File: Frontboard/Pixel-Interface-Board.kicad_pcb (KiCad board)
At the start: 2 copper layers, 29 parts, among them IC1 ATTINY85-P, P1 CONN_02X20, SW1 SW_PUSH, SW10 SW_PUSH, SW11 SW_PUSH, SW12 SW_PUSH, SW2 SW_PUSH, SW3 SW_PUSH, SW4 SW_PUSH, SW5 SW_PUSH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

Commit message: Directories moved, .gitignore added.  Major changes to Frontboard design.  Header was completely backwards, fixed now, pins re-arranged. Table coming shortly.
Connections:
- P1 pad 1: /X -> GND
- P1 pad 10: /R -> (no net)
- P1 pad 11: GND -> (no net)
- P1 pad 13: (no net) -> /Y
- P1 pad 15: (no net) -> /SELECT
- P1 pad 16: GND -> /L
- P1 pad 18: (no net) -> /R
- P1 pad 19: (no net) -> /START
- P1 pad 28: /LEFT -> (no net)
- P1 pad 30: /RIGHT -> GND
- P1 pad 32: GND -> /LEFT
- P1 pad 34: (no net) -> GND
- P1 pad 36: (no net) -> /RIGHT
- P1 pad 4: /START -> (no net)
- P1 pad 6: /SELECT -> (no net)
- P1 pad 7: GND -> /X
- P1 pad 8: /L -> (no net)
- P1 pad 9: /Y -> GND
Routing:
- net /R: track 95.4 -> 333.9 mm
- net GND: track 155.1 -> 55.3 mm
- net /RIGHT: track 137.5 -> 204.8 mm
- net /A: track 118.8 -> 137.4 mm
- net /B: track 123.1 -> 139.0 mm
- net /Y: track 104.4 -> 116.6 mm
- net /L: track 60.7 -> 72.6 mm
- net /LEFT: track 153.3 -> 162.0 mm
- net /START: track 151.1 -> 143.8 mm
- net /SELECT: track 148.8 -> 144.5 mm
- net /X: track 109.8 -> 108.7 mm
- net VDD: track 258.2 -> 257.6 mm
- net /UART_RX: track 36.4 -> 37.1 mm
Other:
- board outline added: 140.2 x 80.3 mm
- net class Default: clearance 0.2 -> 0.4
- rule trace_clearance: 0.2 -> 0.4
- board text added: "DMG-32"
- board text added: "Open Source Hardware and Software"
- board text added: "PyroAVR/DMG-32"
- board text added: "~Andy "PyroAVR" Meyer"

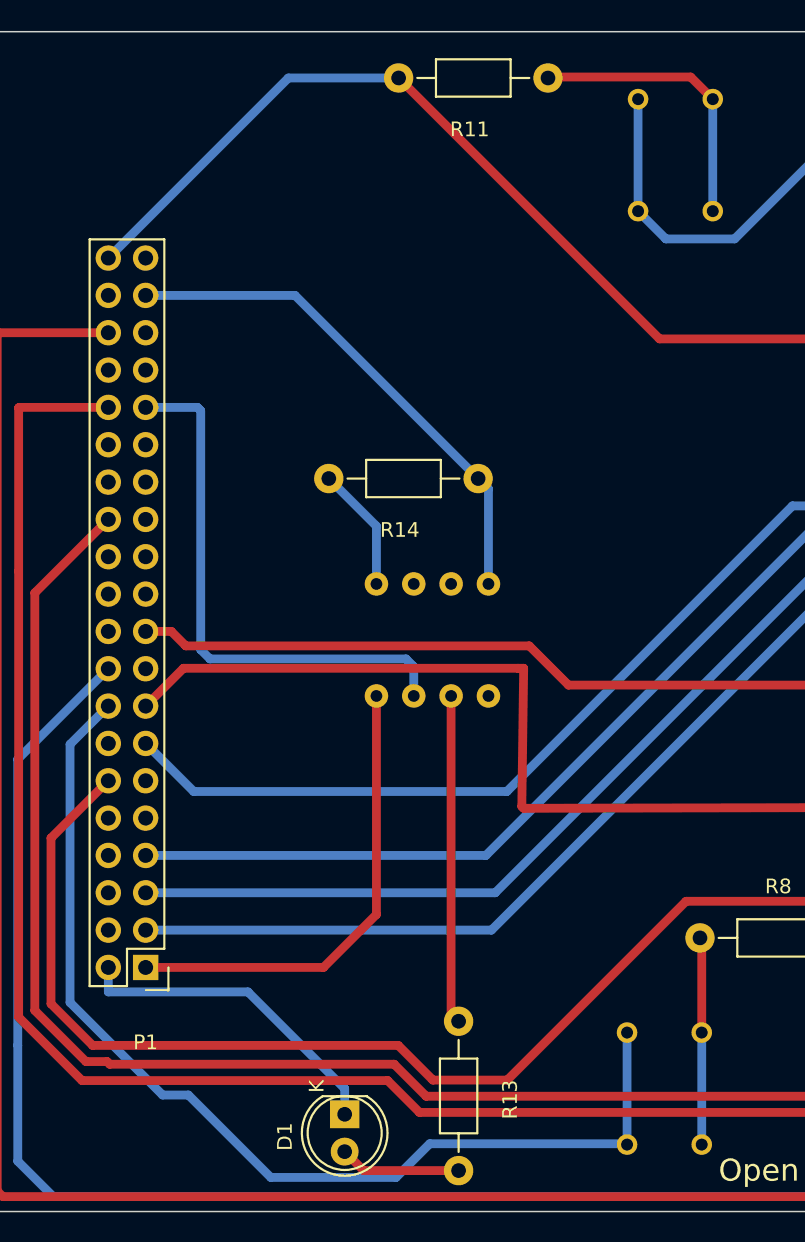
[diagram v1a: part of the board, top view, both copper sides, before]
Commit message: Minor edits to circuitboard front which may help eliminate issues with CAM processing.
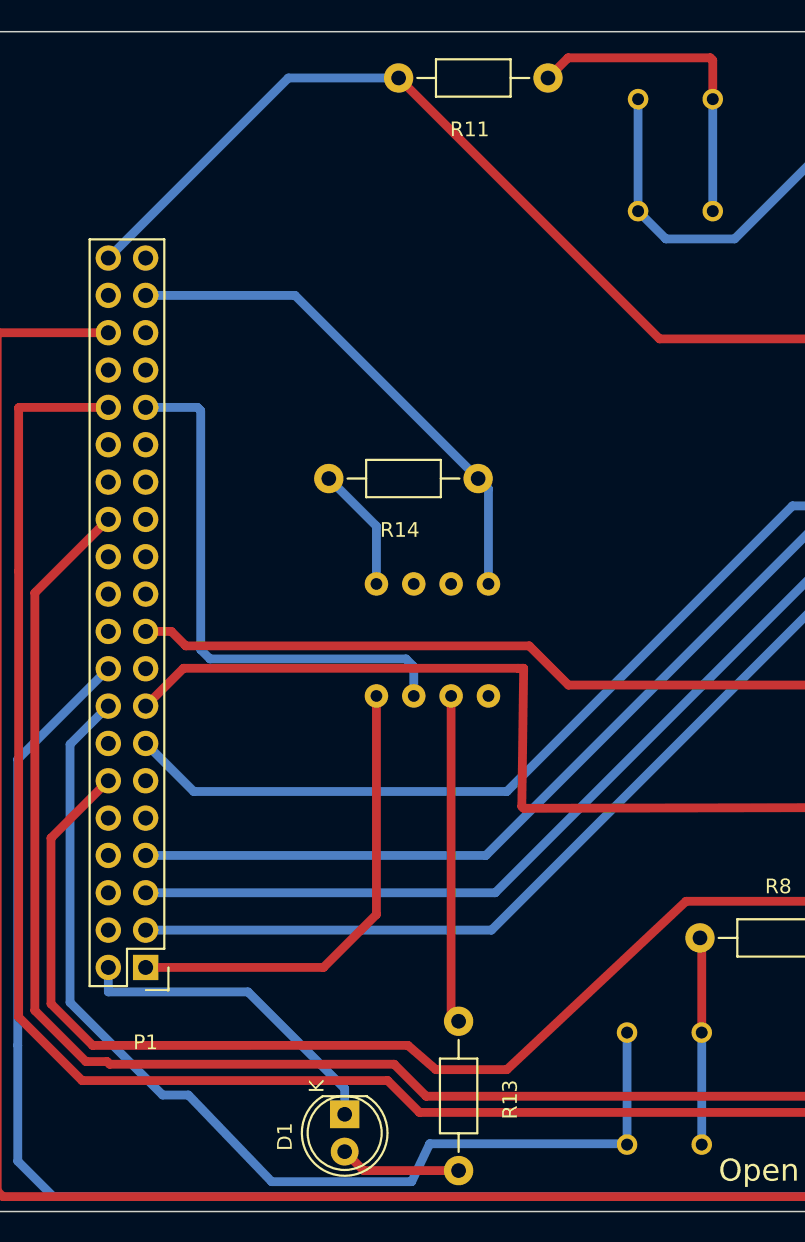
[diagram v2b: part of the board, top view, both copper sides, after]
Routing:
- net Net-(R11-Pad1): track 19.5 -> 22.3 mm
- net /L: track 72.6 -> 73.5 mm
- net /UP: track 122.4 -> 121.6 mm
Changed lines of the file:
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@@
     (thickness 1.6)
     (drawings 12)
-    (tracks 224)
+    (tracks 226)
     (zones 0)
     (modules 29)
@@
   (segment (start 20.066 80.391) (end 20.066 62.834) (width 0.6) (layer B.Cu) (net 12))
   (segment (start 26.3639 86.6889) (end 20.066 80.391) (width 0.6) (layer B.Cu) (net 12))
-  (segment (start 33.7246 92.2944) (end 28.1191 86.6889) (width 0.6) (layer B.Cu) (net 12))
-  (segment (start 42.2447 92.2944) (end 33.7246 92.2944) (width 0.6) (layer B.Cu) (net 12))
-  (segment (start 44.5349 90.0042) (end 42.2447 92.2944) (width 0.6) (layer B.Cu) (net 12))
+  (segment (start 33.782 92.583) (end 28.1191 86.6889) (width 0.6) (layer B.Cu) (net 12))
+  (segment (start 43.307 92.583) (end 33.782 92.583) (width 0.6) (layer B.Cu) (net 12))
+  (segment (start 44.5349 90.0042) (end 43.307 92.583) (width 0.6) (layer B.Cu) (net 12))
   (segment (start 57.96 90.0042) (end 44.5349 90.0042) (width 0.6) (layer B.Cu) (net 12))
   (segment (start 57.96 90.06) (end 57.96 90.0042) (width 0.6) (layer B.Cu) (net 12))
@@
   (segment (start 114.9901 78.898) (end 109.602 73.5099) (width 0.6) (layer B.Cu) (net 15))
   (segment (start 61.9709 73.5099) (end 109.602 73.5099) (width 0.6) (layer F.Cu) (net 15))
-  (segment (start 49.8085 85.6723) (end 61.9709 73.5099) (width 0.6) (layer F.Cu) (net 15))
-  (segment (start 44.7516 85.6723) (end 49.8085 85.6723) (width 0.6) (layer F.Cu) (net 15))
-  (segment (start 42.392 83.3127) (end 44.7516 85.6723) (width 0.6) (layer F.Cu) (net 15))
-  (segment (start 21.6017 83.3127) (end 42.392 83.3127) (width 0.6) (layer F.Cu) (net 15))
+  (segment (start 49.784 84.963) (end 61.9709 73.5099) (width 0.6) (layer F.Cu) (net 15))
+  (segment (start 44.958 84.963) (end 49.784 84.963) (width 0.6) (layer F.Cu) (net 15))
+  (segment (start 43.053 83.312) (end 44.958 84.963) (width 0.6) (layer F.Cu) (net 15))
+  (segment (start 21.6017 83.3127) (end 43.053 83.312) (width 0.6) (layer F.Cu) (net 15))
   (segment (start 18.7706 80.4816) (end 21.6017 83.3127) (width 0.6) (layer F.Cu) (net 15))
   (segment (start 18.7706 69.2094) (end 18.7706 80.4816) (width 0.6) (layer F.Cu) (net 15))
@@
   (segment (start 104.898 31.2401) (end 103.369 29.711) (width 0.6) (layer F.Cu) (net 29))
   (segment (start 103.369 29.711) (end 99.5099 25.852) (width 0.6) (layer F.Cu) (net 29))
+  (segment (start 63.79 18.94) (end 63.79 16.292) (width 0.6) (layer F.Cu) (net 30) (status 400000))
+  (segment (start 53.951 16.129) (end 52.58 17.5) (width 0.6) (layer F.Cu) (net 30) (status 800000))
+  (segment (start 63.627 16.129) (end 53.951 16.129) (width 0.6) (layer F.Cu) (net 30))
+  (segment (start 63.79 16.292) (end 63.627 16.129) (width 0.6) (layer F.Cu) (net 30))
+  (segment (start 52.733 17.653) (end 52.58 17.5) (width 0.6) (layer F.Cu) (net 30))
   (segment (start 63.79 26.56) (end 63.79 18.94) (width 0.6) (layer B.Cu) (net 30))
-  (segment (start 52.6455 17.4345) (end 52.58 17.5) (width 0.6) (layer F.Cu) (net 30))
-  (segment (start 62.2845 17.4345) (end 52.6455 17.4345) (width 0.6) (layer F.Cu) (net 30))
-  (segment (start 63.79 18.94) (end 62.2845 17.4345) (width 0.6) (layer F.Cu) (net 30))
   (segment (start 120.148 73.7401) (end 114.7599 68.352) (width 0.6) (layer B.Cu) (net 31))
   (segment (start 114.5 68.0921) (end 114.5 61.83) (width 0.6) (layer B.Cu) (net 31))

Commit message: Added power port to pcb, rpi micro usb power port no longer used.  Exported new Gerber and Gcode.
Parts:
- added REF**: PINHEAD1-2, Connect:PINHEAD1-2, F.Cu at (17.5, 18.5)
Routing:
- net GND: track 55.3 -> 90.2 mm
- net VCC: track 35.2 -> 52.7 mm
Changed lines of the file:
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@@
 (kicad_pcb (version 4) (host pcbnew "(2015-12-28 BZR 6407, Git 3dff6c0)-product")
   (general
-    (links 76)
+    (links 78)
     (no_connects 10)
-    (area 13.411999 12.365 153.720001 94.67512)
+    (area 12.312905 12.365 153.720001 94.67512)
     (thickness 1.6)
     (drawings 12)
-    (tracks 226)
+    (tracks 236)
     (zones 0)
-    (modules 29)
+    (modules 30)
     (nets 32)
   )
@@
     (mod_text_size 1 1)
     (mod_text_width 0.15)
-    (pad_size 1.5 1.5)
-    (pad_drill 0.6)
+    (pad_size 1.50622 3.01498)
+    (pad_drill 0.99822)
     (pad_to_mask_clearance 0)
     (aux_axis_origin 0 0)
@@
       (drillshape 0)
       (scaleselection 1)
-      (outputdirectory "Gerber Originals/Drill/"))
+      (outputdirectory "Gerber Originals/Drill"))
   )
   (net 0 "")
@@
       (net 14 /R))
   )
+  (module Connect:PINHEAD1-2 (layer F.Cu)
+    (at 17.526 18.542)
+    (attr virtual)
+    (fp_text reference REF** (at 0 -3.9) (layer F.SilkS)
+      (effects (font (size 1 1) (thickness 0.15)))
+    )
+    (fp_text value PINHEAD1-2 (at 0 3.81) (layer F.Fab)
+      (effects (font (size 1 1) (thickness 0.15)))
+    )
+    (fp_line (start 2.54 -1.27) (end -2.54 -1.27) (layer F.SilkS) (width 0.15))
+    (fp_line (start 2.54 3.175) (end -2.54 3.175) (layer F.SilkS) (width 0.15))
+    (fp_line (start -2.54 -3.175) (end 2.54 -3.175) (layer F.SilkS) (width 0.15))
+    (fp_line (start -2.54 -3.175) (end -2.54 3.175) (layer F.SilkS) (width 0.15))
+    (fp_line (start 2.54 -3.175) (end 2.54 3.175) (layer F.SilkS) (width 0.15))
+    (pad 1 thru_hole oval (at -1.27 0) (size 1.50622 3.01498) (drill 0.99822) (layers *.Cu *.Mask)
+      (net 1 GND))
+    (pad 2 thru_hole oval (at 1.27 0) (size 1.50622 3.01498) (drill 0.99822) (layers *.Cu *.Mask)
+      (net 6 VCC))
+  )
   (gr_text PyroAVR/DMG-32 (at 82.423 89.535) (layer F.SilkS)
     (effects (font (size 1.5 1.5) (thickness 0.3)))
@@
   (gr_line (start 153.5372 14.52) (end 13.5372 14.52) (layer Dwgs.User) (width 0.1))
   (gr_line (start 153.5372 94.52) (end 153.5372 14.52) (layer Dwgs.User) (width 0.1))
+  (segment (start 16.256 18.542) (end 16.256 16.129) (width 0.6) (layer F.Cu) (net 1))
+  (segment (start 27.527 34.83) (end 25.21 34.83) (width 0.6) (layer F.Cu) (net 1))
+  (segment (start 27.686 34.671) (end 27.527 34.83) (width 0.6) (layer F.Cu) (net 1))
+  (segment (start 27.686 16.764) (end 27.686 34.671) (width 0.6) (layer F.Cu) (net 1))
+  (segment (start 27.431907 16.033983) (end 27.686 16.764) (width 0.6) (layer F.Cu) (net 1))
+  (segment (start 16.383 16.002) (end 27.431907 16.033983) (width 0.6) (layer F.Cu) (net 1))
+  (segment (start 16.256 16.129) (end 16.383 16.002) (width 0.6) (layer F.Cu) (net 1))
   (segment (start 40.91 59.54) (end 40.91 74.406) (width 0.6) (layer F.Cu) (net 1))
   (segment (start 37.306 78.01) (end 25.21 78.01) (width 0.6) (layer F.Cu) (net 1))
@@
   (segment (start 40.91 47.99) (end 40.91 51.92) (width 0.6) (layer B.Cu) (net 5))
   (segment (start 37.67 44.75) (end 40.91 47.99) (width 0.6) (layer B.Cu) (net 5))
+  (segment (start 18.796 18.542) (end 24.892 18.542) (width 0.6) (layer F.Cu) (net 6))
+  (segment (start 25.21 18.86) (end 25.21 29.75) (width 0.6) (layer F.Cu) (net 6))
+  (segment (start 24.892 18.542) (end 25.21 18.86) (width 0.6) (layer F.Cu) (net 6))
   (segment (start 48.53 45.45) (end 47.83 44.75) (width 0.6) (layer B.Cu) (net 6))
   (segment (start 48.53 51.92) (end 48.53 45.45) (width 0.6) (layer B.Cu) (net 6))
@@
   (segment (start 104.898 31.2401) (end 103.369 29.711) (width 0.6) (layer F.Cu) (net 29))
   (segment (start 103.369 29.711) (end 99.5099 25.852) (width 0.6) (layer F.Cu) (net 29))
-  (segment (start 63.79 18.94) (end 63.79 16.292) (width 0.6) (layer F.Cu) (net 30) (status 400000))
-  (segment (start 53.951 16.129) (end 52.58 17.5) (width 0.6) (layer F.Cu) (net 30) (status 800000))
+  (segment (start 63.79 18.94) (end 63.79 16.292) (width 0.6) (layer F.Cu) (net 30))
+  (segment (start 53.951 16.129) (end 52.58 17.5) (width 0.6) (layer F.Cu) (net 30))
   (segment (start 63.627 16.129) (end 53.951 16.129) (width 0.6) (layer F.Cu) (net 30))
   (segment (start 63.79 16.292) (end 63.627 16.129) (width 0.6) (layer F.Cu) (net 30))
